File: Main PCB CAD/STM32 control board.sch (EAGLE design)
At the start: 113 parts, among them J1 PJ-063BH, J10 S10B-PH, J11 S10B-PH, J12 S10B-PH, J13 S10B-PH, J14 S3B-PH, J15 S3B-PH, J16 S3B-PH, J17 S3B-PH, J18 DG301-4P, J2 S4B-PH, J3 S3B-PH, J4 S3B-PH, J5 S6B-PH, J8 S6B-PH, U1 TPS7A19, U10 STM32G474, U11 DRV8701VIA, U3 L2293Q, U5 REF3330, U6 REF3318, U8 ICM_20600, X1 CSTNE

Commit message: renumbered schematic
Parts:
- removed 5V: (no value), testing:TEST_RING
- removed C100: 100nF, Capacitors:C-EU-CERAMIC0402
- removed C47: 1uF, Capacitors:C-EU-CERAMIC0603
- removed C48, C50: 100nF, Capacitors:C-EU-CERAMIC0603
- removed C49: 10uF, Capacitors:C-EU-CERAMIC1206
- removed C51, C52: 1uF, Capacitors:C-EU-CERAMIC0402
- removed D6: Green, Semiconductor_devices:LED0805
- removed J16, J17: S3B-PH, con-jst-ph:S3B-PH
- removed J18: DG301-4P, Terminal blocks:DG301-4P
- removed R23, R24, R25: 100, Resistors:R-EU0402
- removed S2, S3, S4, S5: B3F-4055, buttons and switches:B3F-4055
- removed TP6: 1.8, testing:TEST_PAD-[1.27MM_SK]
- removed TP7: 3.0, testing:TEST_PAD-[1.27MM_SK]
- removed TP8: 3.3, testing:TEST_PAD-[1.27MM_SK]
- removed U10: STM32G474, stmicroelectronics:STM32G4_LPQFP100
- removed U11: DRV8701VIA, Transistors drivers:DRV8701VIA
- added 1.8: 1.8, testing:TEST_PAD-[1.27MM_SK]
- added 3.0: 3.0, testing:TEST_PAD-[1.27MM_SK]
- added 3V3: (no value), testing:TEST_RING
- added C15, C40: 100nF, Capacitors:C-EU-CERAMIC0402
- added C16, C37: 1uF, Capacitors:C-EU-CERAMIC0402
- added C32: 1uF, Capacitors:C-EU-CERAMIC0603
- added C41, C42: 47uF, Capacitors:C-EU-CERAMIC1210
- added D5: Blue, Semiconductor_devices:LED0805
- added J6, J7, J9: S10B-PH, con-jst-ph:S10B-PH
- added R1: 16k9, Resistors:R-EU0402
- added R19: 100, Resistors:R-EU0402
- added R6: 10K, Resistors:POTEMTIOMETER_EU
- added SW2, SW3, SW4, SW5: B3F-4055, buttons and switches:B3F-4055
- added U4: REF3318, Voltage references:REF33
- added U7: (no value), Current sensing:INA240_TSSOP
- C11, C12, C13, C14, C23: value 4.7uF -> 100nF; device Capacitors:C-EU-CERAMIC0603 -> Capacitors:C-EU-CERAMIC0402
- C20, C4, C5, C6: value 100nF -> 4.7uF; device Capacitors:C-EU-CERAMIC0402 -> Capacitors:C-EU-CERAMIC0603
- C21: value 4.7uF -> 10nF; device Capacitors:C-EU-CERAMIC0603 -> Capacitors:C-EU-CERAMIC0402
- C22: value 10nF -> 100nF
- C26, C31: value 100nF -> 47uF; device Capacitors:C-EU-CERAMIC0402 -> Capacitors:C-EU-CERAMIC1210; MANUFACTURER_PART_NUMBER (none) -> GRM32ER61C476ME15L
- C27, C30: value 100nF -> 10uF; device Capacitors:C-EU-CERAMIC0402 -> Capacitors:C-EU-CERAMIC1206; MANUFACTURER_PART_NUMBER (none) -> CL31B106KOHNNNE
- C28: device Capacitors:C-EU-CERAMIC0402 -> Capacitors:C-EU-CERAMIC0603
- C29: value 1uF -> 100nF; device Capacitors:C-EU-CERAMIC0402 -> Capacitors:C-EU-CERAMIC0603
- C33: value 47uF -> 100nF; device Capacitors:C-EU-CERAMIC1210 -> Capacitors:C-EU-CERAMIC0603; MANUFACTURER_PART_NUMBER GRM32ER61C476ME15L -> (none)
- C34: value 47uF -> 10uF; device Capacitors:C-EU-CERAMIC1210 -> Capacitors:C-EU-CERAMIC1206; MANUFACTURER_PART_NUMBER GRM32ER61C476ME15L -> (none)
- C35: value 10uF -> 100nF; device Capacitors:C-EU-CERAMIC1206 -> Capacitors:C-EU-CERAMIC0603; MANUFACTURER_PART_NUMBER CL31B106KOHNNNE -> (none)
- C36: value 10uF -> 1uF; device Capacitors:C-EU-CERAMIC1206 -> Capacitors:C-EU-CERAMIC0402; MANUFACTURER_PART_NUMBER CL31B106KOHNNNE -> (none)
- C43: value 100nF -> 10uF; device Capacitors:C-EU-CERAMIC0603 -> Capacitors:C-EU-CERAMIC1206; MANUFACTURER_PART_NUMBER (none) -> CL31B106KOHNNNE
- C44: device Capacitors:C-EU-CERAMIC0603 -> Capacitors:C-EU-CERAMIC0402
- C7: value 47uF -> 4.7uF; device Capacitors:C-EU-CERAMIC1210 -> Capacitors:C-EU-CERAMIC0603; MANUFACTURER_PART_NUMBER GRM32ER61C476ME15L -> (none)
- C8: value 47uF -> 100nF; device Capacitors:C-EU-CERAMIC1210 -> Capacitors:C-EU-CERAMIC0402; MANUFACTURER_PART_NUMBER GRM32ER61C476ME15L -> (none)
- C9: value 10uF -> 4.7uF; device Capacitors:C-EU-CERAMIC1206 -> Capacitors:C-EU-CERAMIC0603; MANUFACTURER_PART_NUMBER CL31B106KOHNNNE -> (none)
- D1: value Blue -> Green
- J10, J11, J12, J13: value S10B-PH -> S3B-PH; device con-jst-ph:S10B-PH -> con-jst-ph:S3B-PH
- J14, J4: value S3B-PH -> S6B-PH; device con-jst-ph:S3B-PH -> con-jst-ph:S6B-PH
- J15: value S3B-PH -> DG301-4P; device con-jst-ph:S3B-PH -> Terminal blocks:DG301-4P
- J2: value S4B-PH -> S3B-PH; device con-jst-ph:S4B-PH -> con-jst-ph:S3B-PH
- J3: value S3B-PH -> S4B-PH; device con-jst-ph:S3B-PH -> con-jst-ph:S4B-PH
- J5: value S6B-PH -> S3B-PH; device con-jst-ph:S6B-PH -> con-jst-ph:S3B-PH
- J8: value S6B-PH -> S10B-PH; device con-jst-ph:S6B-PH -> con-jst-ph:S10B-PH
- R11: value 10 mOhm -> 10k; device Resistors:R_EU_CS -> Resistors:R-EU0402; MANUFACTURER_PART_NUMBER STE0805MW75R010F -> (none)
- R13: value 10k -> 10 mOhm; device Resistors:R-EU0402 -> Resistors:R_EU_CS; MANUFACTURER_PART_NUMBER (none) -> STE0805MW75R010F
- R14: value 510k -> 10k
- R15, R9: value 10K -> 10k; device Resistors:POTEMTIOMETER_EU -> Resistors:R-EU0402
- R16: value 10K -> 510k; device Resistors:POTEMTIOMETER_EU -> Resistors:R-EU0402
- R17: value 10k -> 100
- R18: value Calc_needed -> 100
- R2: value 30.9k -> 10k
- R4: value 10k -> Calc_needed
- R5, R7: value 10k -> 10K; device Resistors:R-EU0402 -> Resistors:POTEMTIOMETER_EU
- U1: value TPS7A19 -> STM32G474; device LDOs:TPS7A1901DRBT -> stmicroelectronics:STM32G4_LPQFP100
- U2: value (none) -> TPS7A19; device Current sensing:INA240_TSSOP -> LDOs:TPS7A1901DRBTSON8; MANUFACTURER_PART_NUMBER INA240 -> (none)
- U3: value L2293Q -> REF3330; device Transistors drivers:L2293Q -> Voltage references:REF33
- U5: value REF3330 -> ICM_20600; device Voltage references:REF33 -> InvenSence:ICM_20600
- U6: value REF3318 -> DRV8701VIA; device Voltage references:REF33 -> Transistors drivers:DRV8701VIA
- U8: value ICM_20600 -> L2293Q; device InvenSence:ICM_20600 -> Transistors drivers:L2293Q
- renumbered C53 to C38, C54 to C39, S1 to SW1
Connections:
- net +1.8V: now also 1.8.P$1, C7.1, U4.OUT, U7.REF1, U7.REF2; no longer C14.1, TP6.P$1, U2.REF1, U2.REF2, U6.OUT
- net +3V: now also 3.0.P$1, C5.1, C8.1, R5.1, R6.1, R7.1, U1C.VREF+, U3.OUT; no longer C12.1, C18.1, R15.1, R16.1, R9.1, TP7.P$1, U10C.VREF+, U5.OUT
- net +3V3: now also 3V3.P$1, C10.1, C12.1, C14.1, C15.1, C16.1, C17.1, C19.1, C4.1, C6.1, C9.1, J14.2, J3.1, J4.1, J6.1, J7.1, J9.1, R1.2, R11.2, R12.2, R3.1, R4.2, R9.2, U1C.VBAT, U1C.VDD, U1C.VDDA, U1C.VDD_2, U1C.VDD_3, U1C.VDD_4, U1C.VDD_5, U2.VOUT, U3.IN, U4.IN, U5.VDD, U5.VDDIO, U7.VS; no longer 5V.P$1, C100.1, C22.1, C23.1, C24.1, C25.1, C26.1, C27.1, C28.1, C29.1, C30.1, J14.1, J15.1, J16.1, J17.1, J2.1, J5.2, R17.2, R18.2, R2.2, R4.1, R5.2, R7.2, TP8.P$1, U1.VOUT, U10C.VBAT, U10C.VDD, U10C.VDDA, U10C.VDD_2, U10C.VDD_3, U10C.VDD_4, U10C.VDD_5, U2.VS, U5.IN, U6.IN, U8.VDD, U8.VDDIO
- net AVDD1: now also C36.2, U6.AVDD, U6.VREF; no longer C51.2, U11.AVDD, U11.VREF
- net BRIDGE1_EN: now also R21.1, U1B.PF9; no longer R24.1, U10B.PF9
- net BRIDGE2_EN: now also R22.1, U1B.PF10; no longer R25.1, U10B.PF10
- net DRV2_SNSOUT: now also R15.1, U6.SNSOUT; no longer R13.1, U11.SNSOUT
- net DVDD2: now also C37.2, R14.2, R15.2, U6.DVDD; no longer C52.2, R12.2, R13.2, U11.DVDD
- net ENCODER_1: now also J14.3, U1A.PB4; no longer J5.3, U10A.PB4
- net ENCODER_2: now also J14.4, U1A.PB5; no longer J5.4, U10A.PB5
- net FDCAN2_RX: now also U1A.PB12; no longer U10A.PB12
- net FDCAN2_TX: now also U1A.PB13; no longer U10A.PB13
- net FDCAN_STB: now also U1A.PA12; no longer U10A.PA12
- net GND: now also C15.2, C16.2, C36.1, C37.1, C40.2, C41.2, C42.2, D5.C, J10.3, J11.3, J12.3, J13.3, J14.5, J2.3, J3.4, J4.6, J5.3, J6.2, J7.2, J8.2, J9.2, R16.1, R2.1, R5.3, R6.3, R7.3, SW2.3, SW2.4, SW3.3, SW3.4, SW4.3, SW4.4, SW5.3, SW5.4, U1A.PB8-BOOT0, U1C.VSS, U1C.VSSA, U1C.VSS_2, U1C.VSS_3, U1C.VSS_4, U1C.VSS_5, U2.GND_2, U2.PAD, U4.GND, U5.RESV, U6.GND_2, U6.PAD, U6.SN, U6.SP, U7.GND, U8.GND@1, U8.GND@2, U8.GND@3, U8.GND@4, U8.NC1@2, U8.NC1@3, U8.NC1@4, U8.NC1@5, U8.NC1@6, U8.NC1@7, U8.NC1@8, U8.NC2@1, U8.NC2@18, U8.NC2@19, U8.NC2@20, U8.NC2@21, U8.NC2@22, U8.NC2@23; no longer C100.2, C33.2, C36.2, C49.2, C50.2, C51.1, C52.1, D6.C, J10.2, J11.2, J12.2, J13.2, J14.3, J15.3, J16.3, J17.3, J2.4, J3.3, J4.3, J5.5, J8.6, R14.1, R15.3, R16.3, R3.1, R9.3, S2.3, S2.4, S3.3, S3.4, S4.3, S4.4, S5.3, S5.4, U1.GND, U1.GND_2, U1.PAD, U10A.PB8-BOOT0, U10C.VSS, U10C.VSSA, U10C.VSS_2, U10C.VSS_3, U10C.VSS_4, U10C.VSS_5, U11.GND, U11.GND_2, U11.PAD, U11.SN, U11.SP, U3.GND@1, U3.GND@2, U3.GND@3, U3.GND@4, U3.NC1@2, U3.NC1@3, U3.NC1@4, U3.NC1@5, U3.NC1@6, U3.NC1@7, U3.NC1@8, U3.NC2@1, U3.NC2@18, U3.NC2@19, U3.NC2@20, U3.NC2@21, U3.NC2@22, U3.NC2@23, U8.RESV
- net I2C3_SCL: now also J5.2, U1A.PC8; no longer J4.2, U10A.PC8
- net I2C3_SDA: now also J5.1, U1A.PC9; no longer J4.1, U10A.PC9
- net ICM_CS: now also U1A.PA4, U5.!CS; no longer U10A.PA4, U8.!CS
- net ICM_INT1: now also U1A.PC4, U5.INT1; no longer U10A.PC4, U8.INT1
- net ICM_INT2: now also U1A.PC5, U5.INT2; no longer U10A.PC5, U8.INT2
- net ICM_MISO: now also U1A.PA6, U5.AD0/SDO; no longer U10A.PA6, U8.AD0/SDO
- net ICM_MOSI: now also U1A.PA7, U5.SDA/SDI; no longer U10A.PA7, U8.SDA/SDI
- net ICM_SCK: now also U1A.PA5, U5.SCL/SCLK; no longer U10A.PA5, U8.SCL/SCLK
- net M1: now also J14.1, R13.2, U7.IN+; no longer J5.1, R11.2, U2.IN+
- net M2: now also J14.6, Q4.D; no longer J5.6, Q3.D
- net MOTOR_CS: now also U1A.PB0, U7.OUT; no longer U10A.PB0, U2.OUT
- net M_GH1: now also U6.GH1; no longer U11.GH1
- net M_GH2: now also U6.GH2; no longer U11.GH2
- net M_GL1: now also Q3.G, U6.GL1; no longer Q4.G, U11.GL1
- net M_GL2: now also Q4.G, U6.GL2; no longer Q3.G, U11.GL2
- net M_IN1: now also U1A.PB6, U6.PH_IN1; no longer U10A.PB6, U11.PH_IN1
- net M_IN2: now also U1A.PB7, U6.EN_IN2; no longer U10A.PB7, U11.EN_IN2
- net M_NFAULT: now also R14.1, U1A.PB9, U6.FAULT_N; no longer R12.1, U10A.PB9, U11.FAULT_N
- net M_NSLEEP: now also U1A.PB3, U6.SLEEP_N; no longer U10A.PB3, U11.SLEEP_N
- net M_SH1: now also Q3.D, R13.1, U6.SH1, U7.IN-; no longer Q4.D, R11.1, U11.SH1, U2.IN-
- net M_SH2: now also U6.SH2; no longer U11.SH2
- net N$1: now also U1B.PF0-OSC_IN; no longer U10B.PF0-OSC_IN
- net N$11: now also D2.A; no longer D4.A
- net N$15: now also R18.2, U8.IN2; no longer R22.2, U3.IN2
- net N$16: now also R19.2, U8.IN3; no longer R21.2, U3.IN3
- net N$17: now also C40.1, U8.VSS; no longer C31.1, U3.VSS
- net N$18: now also U8.IN4; no longer U3.IN4
- net N$19: now also R21.2, U8.EN1; no longer R24.2, U3.EN1
- net N$2: now also U1B.PF1-OSC_OUT; no longer U10B.PF1-OSC_OUT
- net N$20: now also R22.2, U8.EN2; no longer R25.2, U3.EN2
- net N$21: now also R1.1, R2.2, U2.FB; no longer R2.1, R3.2, U1.FB
- net N$24: now also C33.1, U6.CPH; no longer C48.1, U11.CPH
- net N$32: now also C33.2, U6.CPL; no longer C48.2, U11.CPL
- net N$33: now also C32.2, U6.VCP; no longer C47.2, U11.VCP
- net N$37: now also R16.2, U6.IDRIVE; no longer R14.2, U11.IDRIVE
- net N$4: now also D5.A; no longer D1.A
- net N$5: now also D4.A; no longer D2.A
- net N$7: now also D1.A, R4.1; no longer D6.A, R18.1
- net N$8: now also R17.2, U8.IN1; no longer R23.2, U3.IN1
- net PA0: now also J10.2, U1A.PA0; no longer J14.2, U10A.PA0
- net PA1: now also J11.2, U1A.PA1; no longer J15.2, U10A.PA1
- net PA2: now also J12.2, U1A.PA2; no longer J16.2, U10A.PA2
- net PA3: now also J13.2, U1A.PA3; no longer J17.2, U10A.PA3
- net PB1: now also U1A.PB1; no longer U10A.PB1
- net PB14: now also C22.1, R9.1, SW2.1, SW2.2, U1A.PB14; no longer C3.1, R10.1, S2.1, S2.2, U10A.PB14
- net PB15: now also C23.1, R10.1, SW3.1, SW3.2, U1A.PB15; no longer C4.1, R5.1, S3.1, S3.2, U10A.PB15
- net PB2: now also U1A.PB2; no longer U10A.PB2
- net PC0: now also R5.2, U1A.PC0; no longer R8.2, U10A.PC0
- net PC1: now also R6.2, U1A.PC1; no longer R9.2, U10A.PC1
- net PC13: now also C24.1, R11.1, SW4.1, SW4.2, U1A.PC13; no longer C5.1, R7.1, S4.1, S4.2, U10A.PC13
- net PC14: now also C25.1, R12.1, SW5.1, SW5.2, U1A.PC14-OSC32_IN; no longer C6.1, R17.1, S5.1, S5.2, U10A.PC14-OSC32_IN
- net PC2: now also R7.2, U1A.PC2; no longer R15.2, U10A.PC2
- net PC3: now also R8.2, U1A.PC3; no longer R16.2, U10A.PC3
- net PC6: now also U1A.PC6; no longer U10A.PC6
- net PC7: now also U1A.PC7; no longer U10A.PC7
- net PD0: now also J6.3, U1A.PD0; no longer J10.3, U10A.PD0
- net PD1: now also J6.4, U1A.PD1; no longer J10.4, U10A.PD1
- net PD10: now also J7.5, U1A.PD10; no longer J11.5, U10A.PD10
- net PD11: now also J7.6, U1A.PD11; no longer J11.6, U10A.PD11
- net PD12: now also J7.7, U1A.PD12; no longer J11.7, U10A.PD12
- net PD13: now also J7.8, U1A.PD13; no longer J11.8, U10A.PD13
- net PD14: now also J7.9, U1A.PD14; no longer J11.9, U10A.PD14
- net PD15: now also J7.10, U1A.PD15; no longer J11.10, U10A.PD15
- net PD2: now also J6.5, U1A.PD2; no longer J10.5, U10A.PD2
- net PD3: now also J6.6, U1A.PD3; no longer J10.6, U10A.PD3
- net PD4: now also J6.7, U1A.PD4; no longer J10.7, U10A.PD4
- net PD5: now also J6.8, U1A.PD5; no longer J10.8, U10A.PD5
- net PD6: now also J6.9, U1A.PD6; no longer J10.9, U10A.PD6
- net PD7: now also J6.10, U1A.PD7; no longer J10.10, U10A.PD7
- net PD8: now also J7.3, U1A.PD8; no longer J11.3, U10A.PD8
- net PD9: now also J7.4, U1A.PD9; no longer J11.4, U10A.PD9
- net PE0: now also J8.3, U1B.PE0; no longer J12.3, U10B.PE0
- net PE1: now also J8.4, U1B.PE1; no longer J12.4, U10B.PE1
- net PE10: now also J9.5, U1B.PE10; no longer J13.5, U10B.PE10
- net PE11: now also J9.6, U1B.PE11; no longer J13.6, U10B.PE11
- net PE12: now also J9.7, U1B.PE12; no longer J13.7, U10B.PE12
- net PE13: now also J9.8, U1B.PE13; no longer J13.8, U10B.PE13
- net PE14: now also J9.9, U1B.PE14; no longer J13.9, U10B.PE14
- net PE15: now also J9.10, U1B.PE15; no longer J13.10, U10B.PE15
- net PE2: now also J8.5, U1B.PE2; no longer J12.5, U10B.PE2
- net PE3: now also J8.6, U1B.PE3; no longer J12.6, U10B.PE3
- net PE4: now also J8.7, U1B.PE4; no longer J12.7, U10B.PE4
- net PE5: now also J8.8, U1B.PE5; no longer J12.8, U10B.PE5
- net PE6: now also J8.9, U1B.PE6; no longer J12.9, U10B.PE6
- net PE7: now also J8.10, U1B.PE7; no longer J12.10, U10B.PE7
- net PE8: now also J9.3, U1B.PE8; no longer J13.3, U10B.PE8
- net PE9: now also J9.4, U1B.PE9; no longer J13.4, U10B.PE9
- net POUT1: now also J15.1, U8.OUT1; no longer J18.1, U3.OUT1
- net POUT2: now also J15.2, U8.OUT2; no longer J18.2, U3.OUT2
- net POUT3: now also J15.3, U8.OUT3; no longer J18.3, U3.OUT3
- net POUT4: now also J15.4, U8.OUT4; no longer J18.4, U3.OUT4
- net POWER_OUT1: now also R17.1, U1A.PA8; no longer R23.1, U10A.PA8
- net POWER_OUT2: now also R18.1, U1A.PA9; no longer R22.1, U10A.PA9
- net POWER_OUT3: now also R19.1, U1A.PA10; no longer R21.1, U10A.PA10
- net POWER_OUT4: now also U1A.PA11; no longer U10A.PA11
- net REG: now also C18.1, U5.REGOUT; no longer C19.1, U8.REGOUT
- net RST: now also C3.1, R3.2, U1B.PG10-NRST; no longer C10.1, R4.2, U10B.PG10-NRST
- net SPI3_MISO: now also J4.3, U1A.PC11; no longer J8.3, U10A.PC11
- net SPI3_MOSI: now also J4.2, U1A.PC12; no longer J8.2, U10A.PC12
- net SPI3_SCK: now also J4.4, U1A.PC10; no longer J8.4, U10A.PC10
- net SPI_CS: now also J4.5, U1A.PA15; no longer J8.5, U10A.PA15
- net SWCLK: now also J3.3, U1A.PA14; no longer J2.3, U10A.PA14
- net SWDIO: now also J3.2, U1A.PA13; no longer J2.2, U10A.PA13
- net USART3_RX: now also J2.2, U1A.PB11; no longer J3.2, U10A.PB11
- net USART3_TX: now also J2.1, U1A.PB10; no longer J3.1, U10A.PB10
- net VDD: now also C26.1, C27.1, C28.1, C29.1, C30.1, C31.1, C32.1, C41.1, C42.1, U2.EN, U2.VIN, U6.VM, U8.VS, U8.VS@1; no longer C17.1, C33.1, C36.1, C47.1, C49.1, C50.1, C7.1, C8.1, C9.1, U1.EN, U1.VIN, U11.VM, U3.VS, U3.VS@1
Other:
- note added: "Calculated output voltage is 3.317 V. Tolerance of resistors in FB voltage divider is 1%"
- note added: "Grid size 0.05 inch, Alt 0.01 inch"
- note added: "Schematic designed to work either from external power adapter (from 12V to 5V) or from ST-Link 3.3V power line"
- note removed: "Возможно надо будет заменить С1 на меньшей номинал при составлении спецификации. Нам необходимо 10uF на напряжение входного питния до 12.6В, то есть конденсаторы 16В либо 25В."
- note removed: "Гироскоп-акселлерометр"
- note removed: "Драйвер двигателя постоянного тока"
- note removed: "Микроконтроллер и базовые интерфейсы"
- note removed: "Пересчитать"
- note removed: "Питание"
- note removed: "Полупорты и разъемы для аналоговых датчиков"
- note removed: "Пользовательские кнопки"
- note removed: "Потенциометры"
- note removed: "Расчетное выходное напряжение равно 5.04в Резисторы в делителе с точностью 0.1%"
- note removed: "Светодиоды"
- note removed: "Сетка 0.05 inch - основной шаг, 0.01 inch - Alt-шаг"

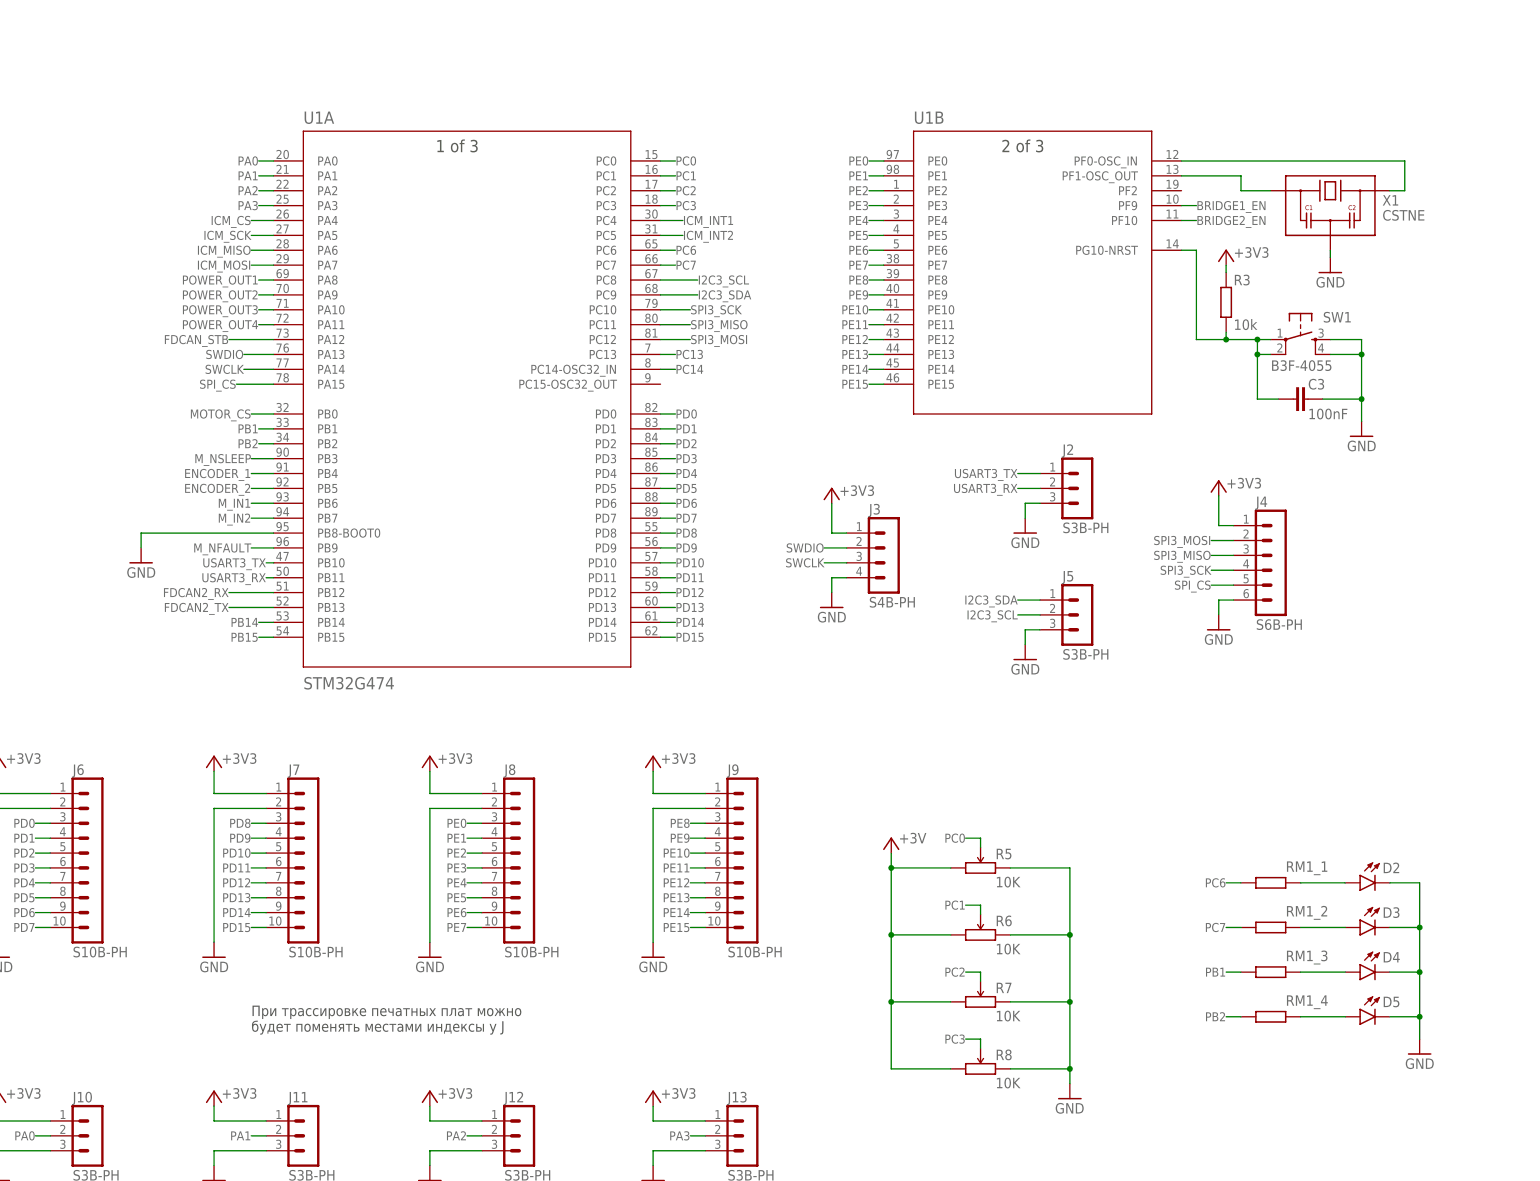
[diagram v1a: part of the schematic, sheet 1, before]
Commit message: Can removed
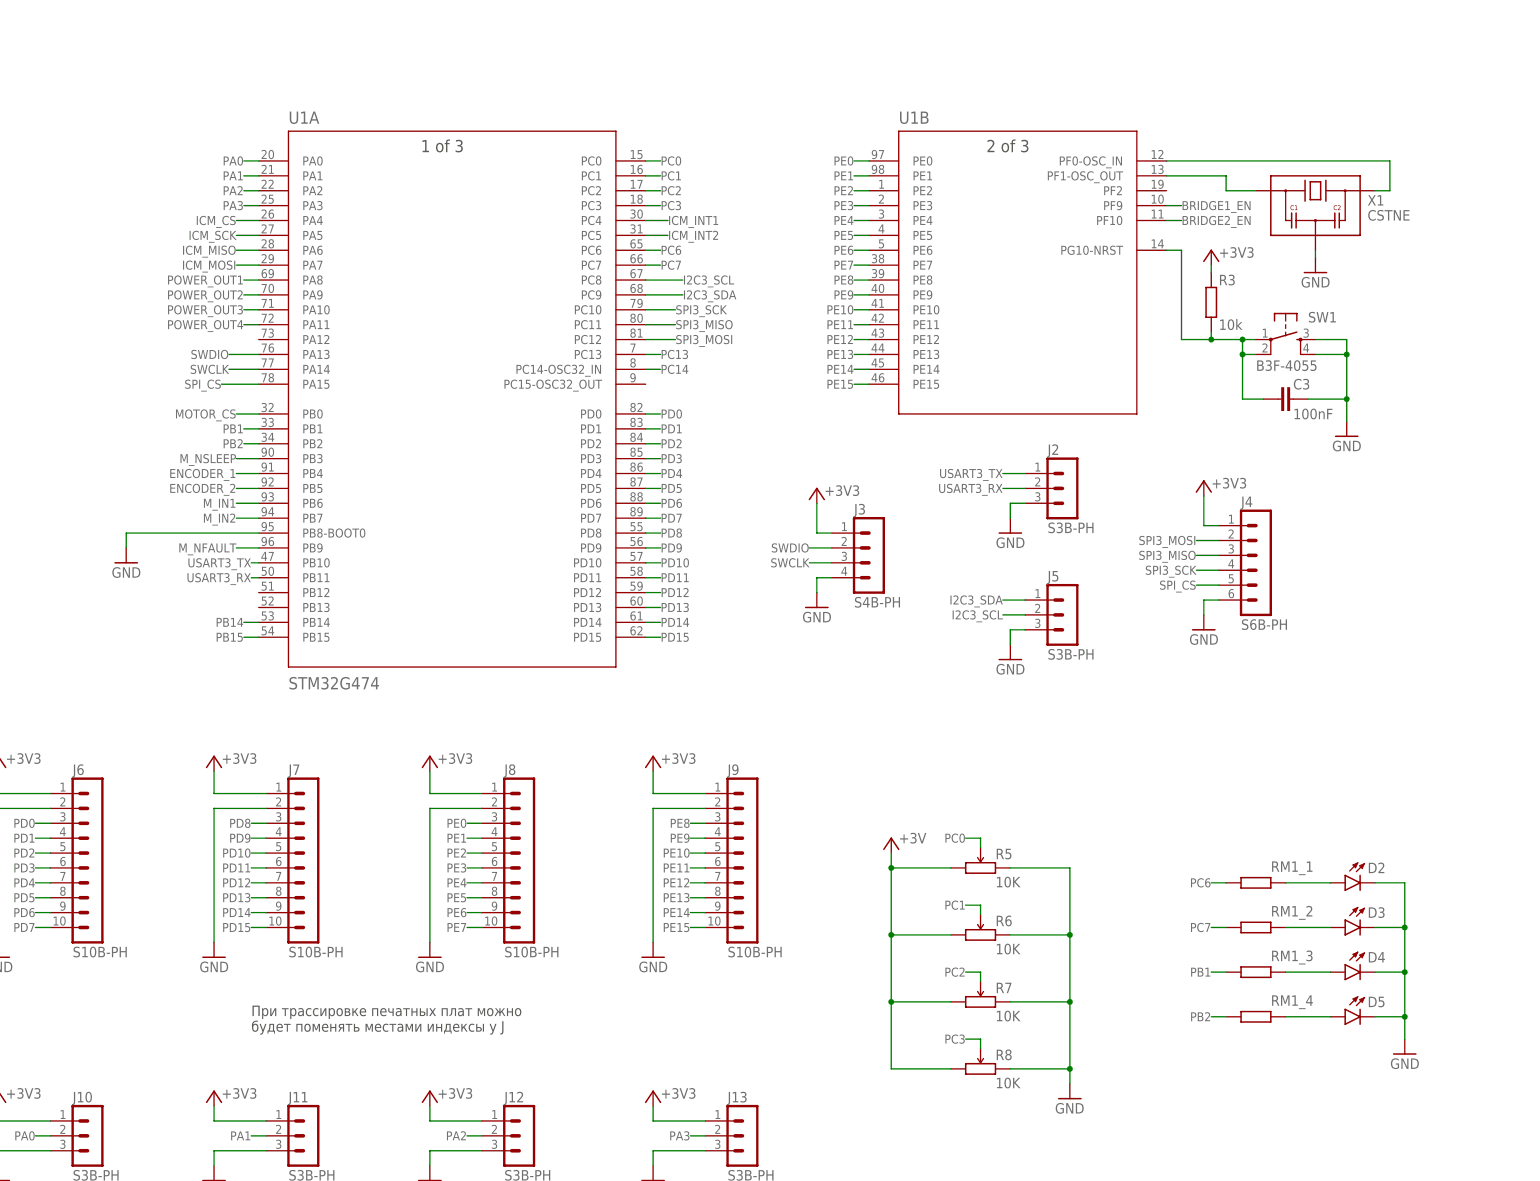
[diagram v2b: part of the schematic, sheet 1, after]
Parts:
- C1: MANUFACTURER_PART_NUMBER (none) -> CL31B106KOHNNNE
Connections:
- removed net FDCAN2_RX: U1A.PB12
- removed net FDCAN2_TX: U1A.PB13
- removed net FDCAN_STB: U1A.PA12
- removed net M2: J14.6, Q2.S, Q4.D
- net M_SH2: now also J14.6, Q2.S, Q4.D
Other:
- moved on the sheet: C3, D2, D3, D4, D5, J2, J3, J4, J5, R3, RM1_1, RM1_2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

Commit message: for BOM review
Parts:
- added C45, C46, C47, C48: 22uF, Capacitors:C-EU-CERAMIC1210
- added C49: 10uF, Capacitors:C-EU-CERAMIC1206
- added C50: 100nF, Capacitors:C-EU-CERAMIC0402
- C1, C30: MANUFACTURER_PART_NUMBER CL31B106KOHNNNE -> CL31B106KAHNNNE
- C11, C22, C8: value 100nF -> 4.7uF; device Capacitors:C-EU-CERAMIC0402 -> Capacitors:C-EU-CERAMIC0603
- C16, C37: value 1uF -> 100nF
- C18, C40: value 100nF -> 1uF; device Capacitors:C-EU-CERAMIC0402 -> Capacitors:C-EU-CERAMIC0603
- C2: value 47uF -> 22uF
- C20, C5: value 4.7uF -> 100nF; device Capacitors:C-EU-CERAMIC0603 -> Capacitors:C-EU-CERAMIC0402
- C21: value 10nF -> 100nF
- C23: value 100nF -> 10nF
- C26, C31, C42: value 47uF -> 100nF; device Capacitors:C-EU-CERAMIC1210 -> Capacitors:C-EU-CERAMIC0402; MANUFACTURER_PART_NUMBER GRM32ER61C476ME15L -> (none)
- C27, C43: value 10uF -> 100nF; device Capacitors:C-EU-CERAMIC1206 -> Capacitors:C-EU-CERAMIC0402; MANUFACTURER_PART_NUMBER CL31B106KOHNNNE -> (none)
- C28, C29, C35: value 100nF -> 22uF; device Capacitors:C-EU-CERAMIC0603 -> Capacitors:C-EU-CERAMIC1210; MANUFACTURER_PART_NUMBER (none) -> GRM32ER61C476ME15L
- C3: value 100nF -> 22uF; device Capacitors:C-EU-CERAMIC0402 -> Capacitors:C-EU-CERAMIC1210; MANUFACTURER_PART_NUMBER (none) -> GRM32ER61C476ME15L
- C32: value 1uF -> 100nF; device Capacitors:C-EU-CERAMIC0603 -> Capacitors:C-EU-CERAMIC0402
- C33: value 100nF -> 10uF; device Capacitors:C-EU-CERAMIC0603 -> Capacitors:C-EU-CERAMIC1206; MANUFACTURER_PART_NUMBER (none) -> CL31B106KAHNNNE
- C34: value 10uF -> 22uF; device Capacitors:C-EU-CERAMIC1206 -> Capacitors:C-EU-CERAMIC1210; MANUFACTURER_PART_NUMBER (none) -> GRM32ER61C476ME15L
- C36: device Capacitors:C-EU-CERAMIC0402 -> Capacitors:C-EU-CERAMIC0603
- C38: value 100nF -> 10uF; device Capacitors:C-EU-CERAMIC0402 -> Capacitors:C-EU-CERAMIC1206; MANUFACTURER_PART_NUMBER (none) -> CL31B106KAHNNNE
- C4: value 4.7uF -> 10uF; device Capacitors:C-EU-CERAMIC0603 -> Capacitors:C-EU-CERAMIC1206; MANUFACTURER_PART_NUMBER (none) -> CL31B106KAHNNNE
- C41: value 47uF -> 1uF; device Capacitors:C-EU-CERAMIC1210 -> Capacitors:C-EU-CERAMIC0603; MANUFACTURER_PART_NUMBER GRM32ER61C476ME15L -> (none)
- R13: MANUFACTURER_PART_NUMBER STE0805MW75R010F -> ERJ6CWDR010V
- R4: value Calc_needed -> 10k
- RM1: value RES_ARRAY -> RES_ARRAY0402_YAGEO; device Resistors:RES_ARRAY -> Resistors:RES_ARRAY0402_YAGEO
- renumbered 1.8 to TP5, 3.0 to TP4, 3V3 to TP1, GND to TP3, VIN to TP2
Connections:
- net +1.8V: now also C42.1, C9.1; no longer C38.1, C7.1
- net +3V: now also C10.1, C7.1; no longer C5.1, C8.1
- net +3V3: now also C18.1, C22.1, C23.1, C3.1, C43.1, C8.1; no longer C10.1, C20.1, C39.1, C9.1
- net AVDD1: now also C40.2; no longer C36.2
- net DVDD2: now also C41.2; no longer C37.2
- net GND: now also C32.2, C33.2, C40.1, C41.1, C45.2, C46.2, C47.2, C48.2, C49.2, C50.2; no longer C36.1, C37.1, C40.2, C41.2
- net N$17: now also C44.1; no longer C40.1
- net N$24: now also C37.1; no longer C33.1
- net N$32: now also C37.2; no longer C33.2
- net N$33: now also C36.2; no longer C32.2
- net PB14: now also C24.1; no longer C22.1
- net PB15: now also C25.1; no longer C23.1
- net PC13: now also C26.1; no longer C24.1
- net PC14: now also C27.1; no longer C25.1
- net REG: now also C20.1; no longer C18.1
- net RST: now also C5.1; no longer C3.1
- net VDD: now also C33.1, C36.1, C38.1, C39.1, C45.1, C46.1, C47.1, C48.1, C49.1, C50.1; no longer C26.1, C27.1, C41.1, C42.1, C43.1, C44.1
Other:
- moved on the sheet: C10, C11, C12, C13, C14, C15, C16, C17, C18, C19, C20, C21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
